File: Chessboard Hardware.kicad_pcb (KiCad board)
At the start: 2 copper layers, 200 x 200 mm, 86 parts, among them J1 Conn_01x04_Pin

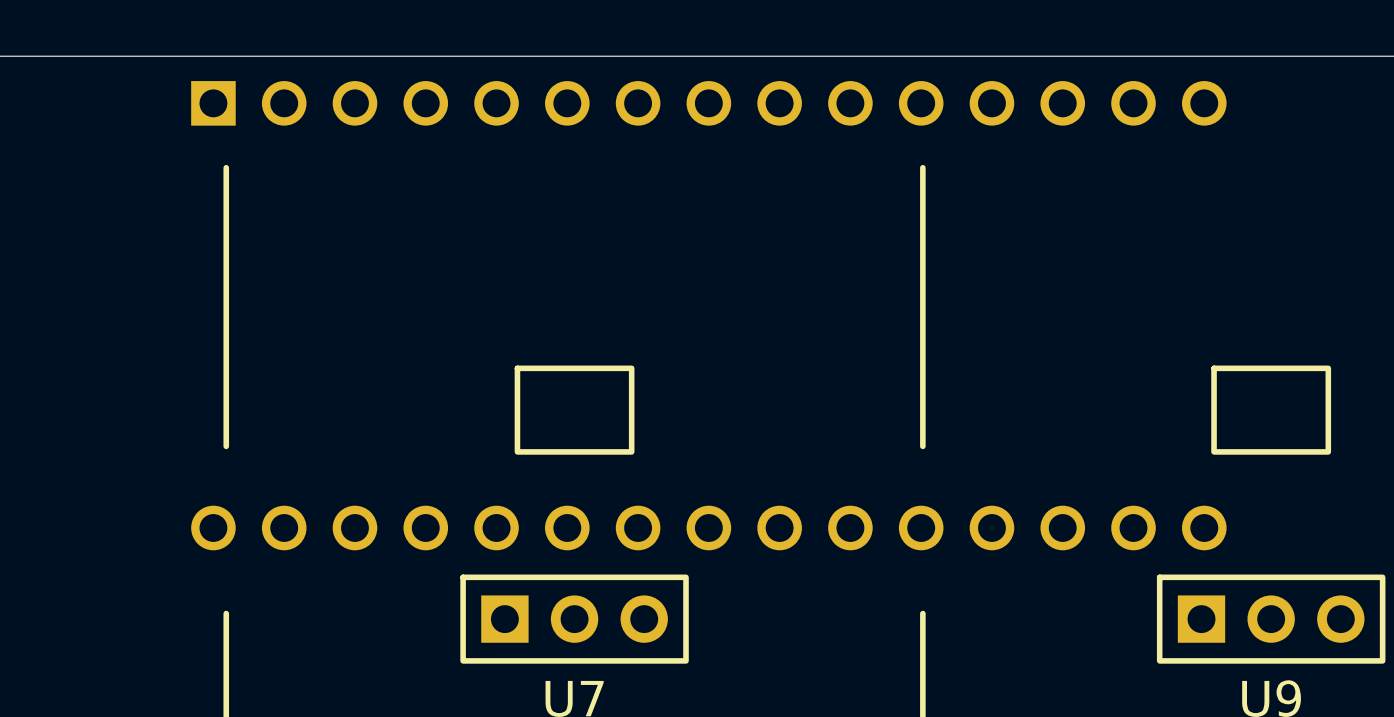
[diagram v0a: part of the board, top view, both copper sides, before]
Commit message: Fix Arduino Nano position
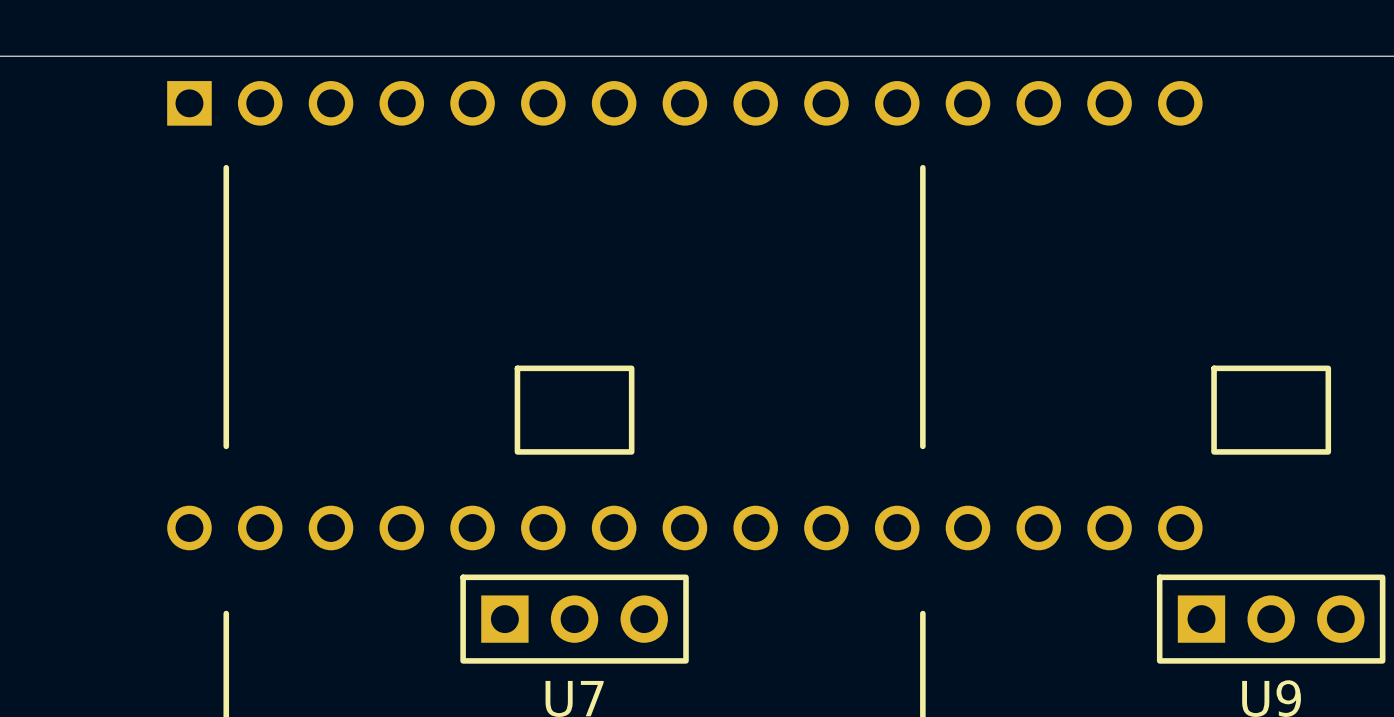
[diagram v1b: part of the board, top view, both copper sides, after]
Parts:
- moved A1 0.86 mm to (198.7, 51.7)
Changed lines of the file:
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@@
 	(footprint "Project Library:Arduino_Nano"
 		(layer "B.Cu")
-		(at 199.54 51.69 -90)
+		(at 198.68 51.69 -90)
 		(descr "Arduino Nano, http://www.mouser.com/pdfdocs/Gravitech_Arduino_Nano3_0.pdf")
 		(tags "Arduino Nano")

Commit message: Start routing
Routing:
- net GND: track 0.00 -> 1874.6 mm, vias 0 -> 1
- net VCC: track 0.00 -> 1793.3 mm
- net /INH: track 0.00 -> 305.9 mm
- net /C: track 0.00 -> 294.0 mm, vias 0 -> 7
- net /B: track 0.00 -> 281.8 mm, vias 0 -> 7
- net /A: track 0.00 -> 280.1 mm
- net /TX: track 0.00 -> 55.8 mm, vias 0 -> 1
- net /RX: track 0.00 -> 52.2 mm, vias 0 -> 1

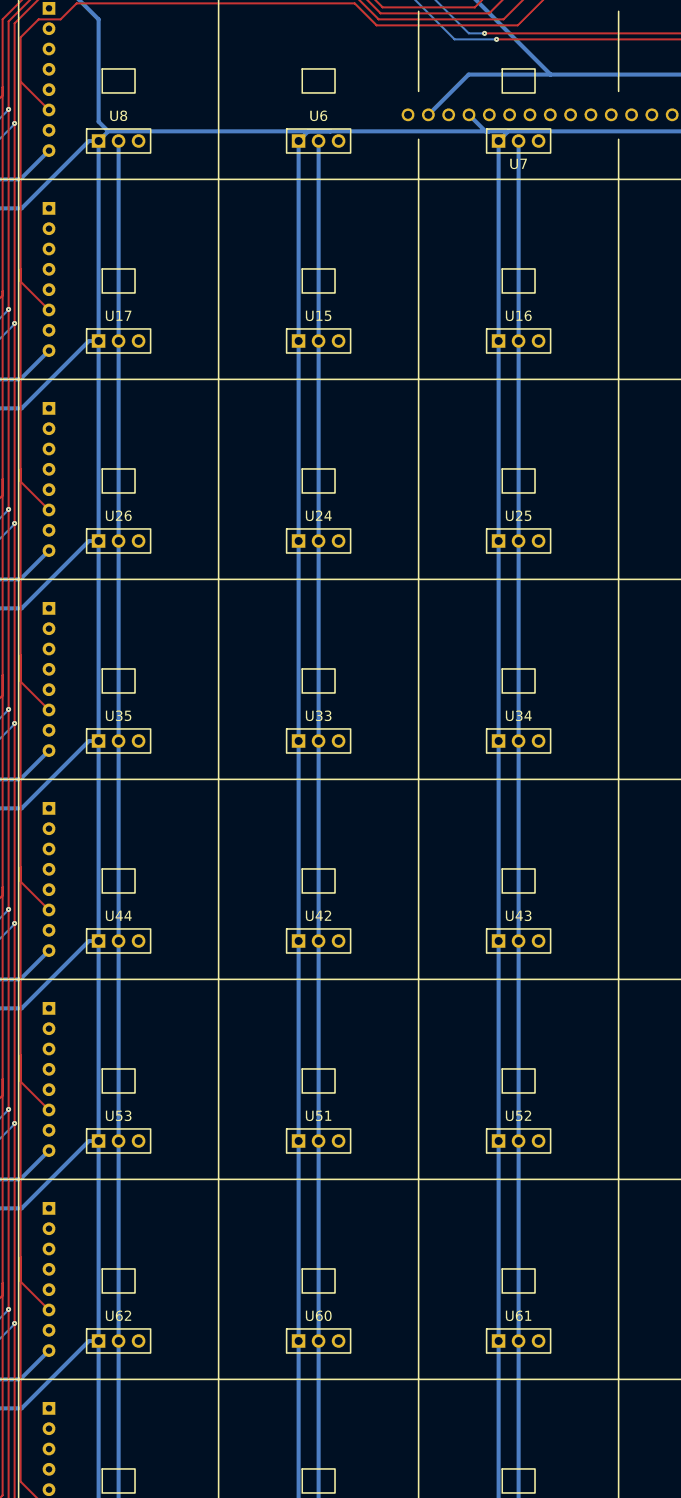
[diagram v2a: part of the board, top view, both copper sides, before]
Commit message: Route signal lines
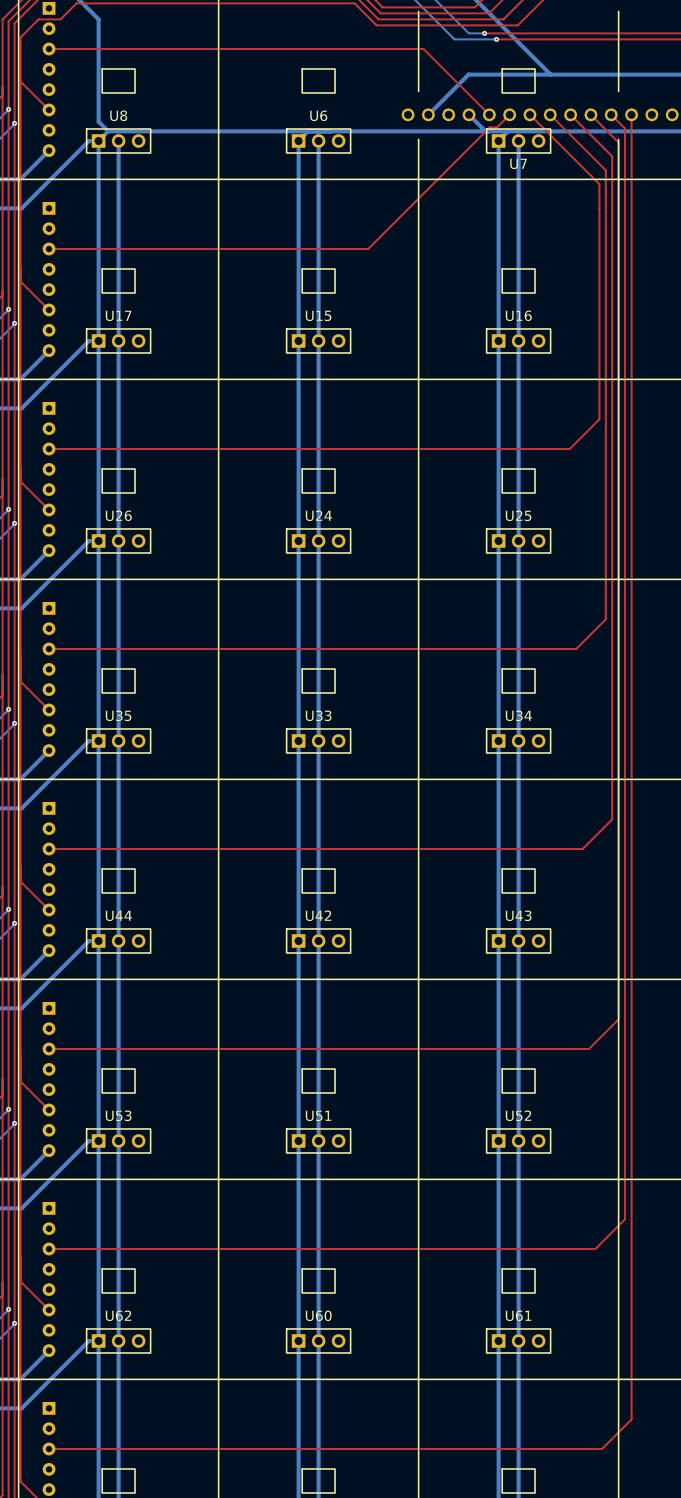
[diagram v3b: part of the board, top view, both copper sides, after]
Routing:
- net /COM7: track 0.00 -> 237.4 mm
- net /COM6: track 0.00 -> 212.3 mm
- net /COM5: track 0.00 -> 187.2 mm
- net /COM4: track 0.00 -> 162.2 mm
- net /COM3: track 0.00 -> 137.1 mm
- net /COM2: track 0.00 -> 112.0 mm
- net /COM1: track 0.00 -> 64.5 mm
- net /COM0: track 0.00 -> 58.4 mm
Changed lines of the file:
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@@
+	)
+	(segment
+		(start 226.62 66.93)
+		(end 226.62 230)
+		(width 0.254)
+		(layer "F.Cu")
+		(net 3)
+	)
+	(segment
+		(start 153.8 233.705)
+		(end 222.915 233.705)
+		(width 0.254)
+		(layer "F.Cu")
+		(net 3)
+	)
+	(segment
+		(start 222.915 233.705)
+		(end 226.62 230)
+		(width 0.254)
+		(layer "F.Cu")
+		(net 3)
+	)
+	(segment
+		(start 211.38 66.93)
+		(end 209.81 68.5)
+		(width 0.254)
+		(layer "F.Cu")
+		(net 5)
+	)
+	(segment
+		(start 208.9 68.5)
+		(end 193.695 83.705)
+		(width 0.254)
+		(layer "F.Cu")
+		(net 5)
+	)
+	(segment
+		(start 193.695 83.705)
+		(end 153.8 83.705)
+		(width 0.254)
+		(layer "F.Cu")
+		(net 5)
+	)
+	(segment
+		(start 209.81 68.5)
+		(end 208.9 68.5)
+		(width 0.254)
+		(layer "F.Cu")
+		(net 5)
+	)
+	(segment
+		(start 219 66.93)
+		(end 224.2 72.13)
+		(width 0.254)
+		(layer "F.Cu")
+		(net 7)
+	)
+	(segment
+		(start 224.2 76.5)
+		(end 224.2 155)
+		(width 0.254)
+		(layer "F.Cu")
+		(net 7)
+	)
+	(segment
+		(start 224.2 72.13)
+		(end 224.2 76.5)
+		(width 0.254)
+		(layer "F.Cu")
+		(net 7)
+	)
+	(segment
+		(start 220.495 158.705)
+		(end 224.2 155)
+		(width 0.254)
+		(layer "F.Cu")
+		(net 7)
+	)
+	(segment
+		(start 153.8 158.705)
+		(end 220.495 158.705)
+		(width 0.254)
+		(layer "F.Cu")
+		(net 7)
 	)
 	(segment
@@
 	)
 	(segment
+		(start 221.295 183.705)
+		(end 225 180)
+		(width 0.254)
+		(layer "F.Cu")
+		(net 15)
+	)
+	(segment
+		(start 225 70.39)
+		(end 225 77.2)
+		(width 0.254)
+		(layer "F.Cu")
+		(net 15)
+	)
+	(segment
+		(start 225 77.2)
+		(end 225 180)
+		(width 0.254)
+		(layer "F.Cu")
+		(net 15)
+	)
+	(segment
+		(start 221.54 66.93)
+		(end 225 70.39)
+		(width 0.254)
+		(layer "F.Cu")
+		(net 15)
+	)
+	(segment
+		(start 153.8 183.705)
+		(end 221.295 183.705)
+		(width 0.254)
+		(layer "F.Cu")
+		(net 15)
+	)
+	(segment
 		(start 152.75 52.25)
 		(end 192.25 52.25)
@@
 	)
 	(segment
+		(start 153.8 208.705)
+		(end 222.095 208.705)
+		(width 0.254)
+		(layer "F.Cu")
+		(net 19)
+	)
+	(segment
+		(start 224.08 66.93)
+		(end 225.8 68.65)
+		(width 0.254)
+		(layer "F.Cu")
+		(net 19)
+	)
+	(segment
+		(start 222.095 208.705)
+		(end 225.8 205)
+		(width 0.254)
+		(layer "F.Cu")
+		(net 19)
+	)
+	(segment
+		(start 225.8 68.65)
+		(end 225.8 75.7)
+		(width 0.254)
+		(layer "F.Cu")
+		(net 19)
+	)
+	(segment
+		(start 225.8 75.7)
+		(end 225.8 205)
+		(width 0.254)
+		(layer "F.Cu")
+		(net 19)
+	)
+	(segment
+		(start 208.84 66.93)
+		(end 200.615 58.705)
+		(width 0.254)
+		(layer "F.Cu")
+		(net 20)
+	)
+	(segment
+		(start 200.615 58.705)
+		(end 153.8 58.705)
+		(width 0.254)
+		(layer "F.Cu")
+		(net 20)
+	)
+	(segment
 		(start 148 163.5)
 		(end 148 137)
@@
 		(net 24)
 	)
+	(segment
+		(start 153.8 108.705)
+		(end 218.895 108.705)
+		(width 0.254)
+		(layer "F.Cu")
+		(net 26)
+	)
+	(segment
+		(start 218.895 108.705)
+		(end 222.6 105)
+		(width 0.254)
+		(layer "F.Cu")
+		(net 26)
+	)
+	(segment
+		(start 222.6 78.7)
+		(end 222.6 105)
+		(width 0.254)
+		(layer "F.Cu")
+		(net 26)
+	)
+	(segment
+		(start 213.92 66.93)
+		(end 222.6 75.61)
+		(width 0.254)
+		(layer "F.Cu")
+		(net 26)
+	)
+	(segment
+		(start 222.6 75.61)
+		(end 222.6 78.7)
+		(width 0.254)
+		(layer "F.Cu")
+		(net 26)
+	)
+	(segment
+		(start 153.8 133.705)
+		(end 219.695 133.705)
+		(width 0.254)
+		(layer "F.Cu")
+		(net 28)
+	)
+	(segment
+		(start 219.695 133.705)
+		(end 223.4 130)
+		(width 0.254)
+		(layer "F.Cu")
+		(net 28)
+	)
+	(segment
+		(start 223.4 76.7)
+		(end 223.4 130)
+		(width 0.254)
+		(layer "F.Cu")
+		(net 28)
+	)
+	(segment
+		(start 216.46 66.93)
+		(end 223.4 73.87)
+		(width 0.254)
+		(layer "F.Cu")
+		(net 28)
+	)
+	(segment
+		(start 223.4 73.87)
+		(end 223.4 76.7)
+		(width 0.254)
+		(layer "F.Cu")
+		(net 28)
+	)
 )
